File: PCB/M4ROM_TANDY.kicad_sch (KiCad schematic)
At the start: 7 parts, among them J1 Tandy_100_102_200_option_rom, J2 4ROM_prog_female, SW1 CUS-14TB, U1 29F010

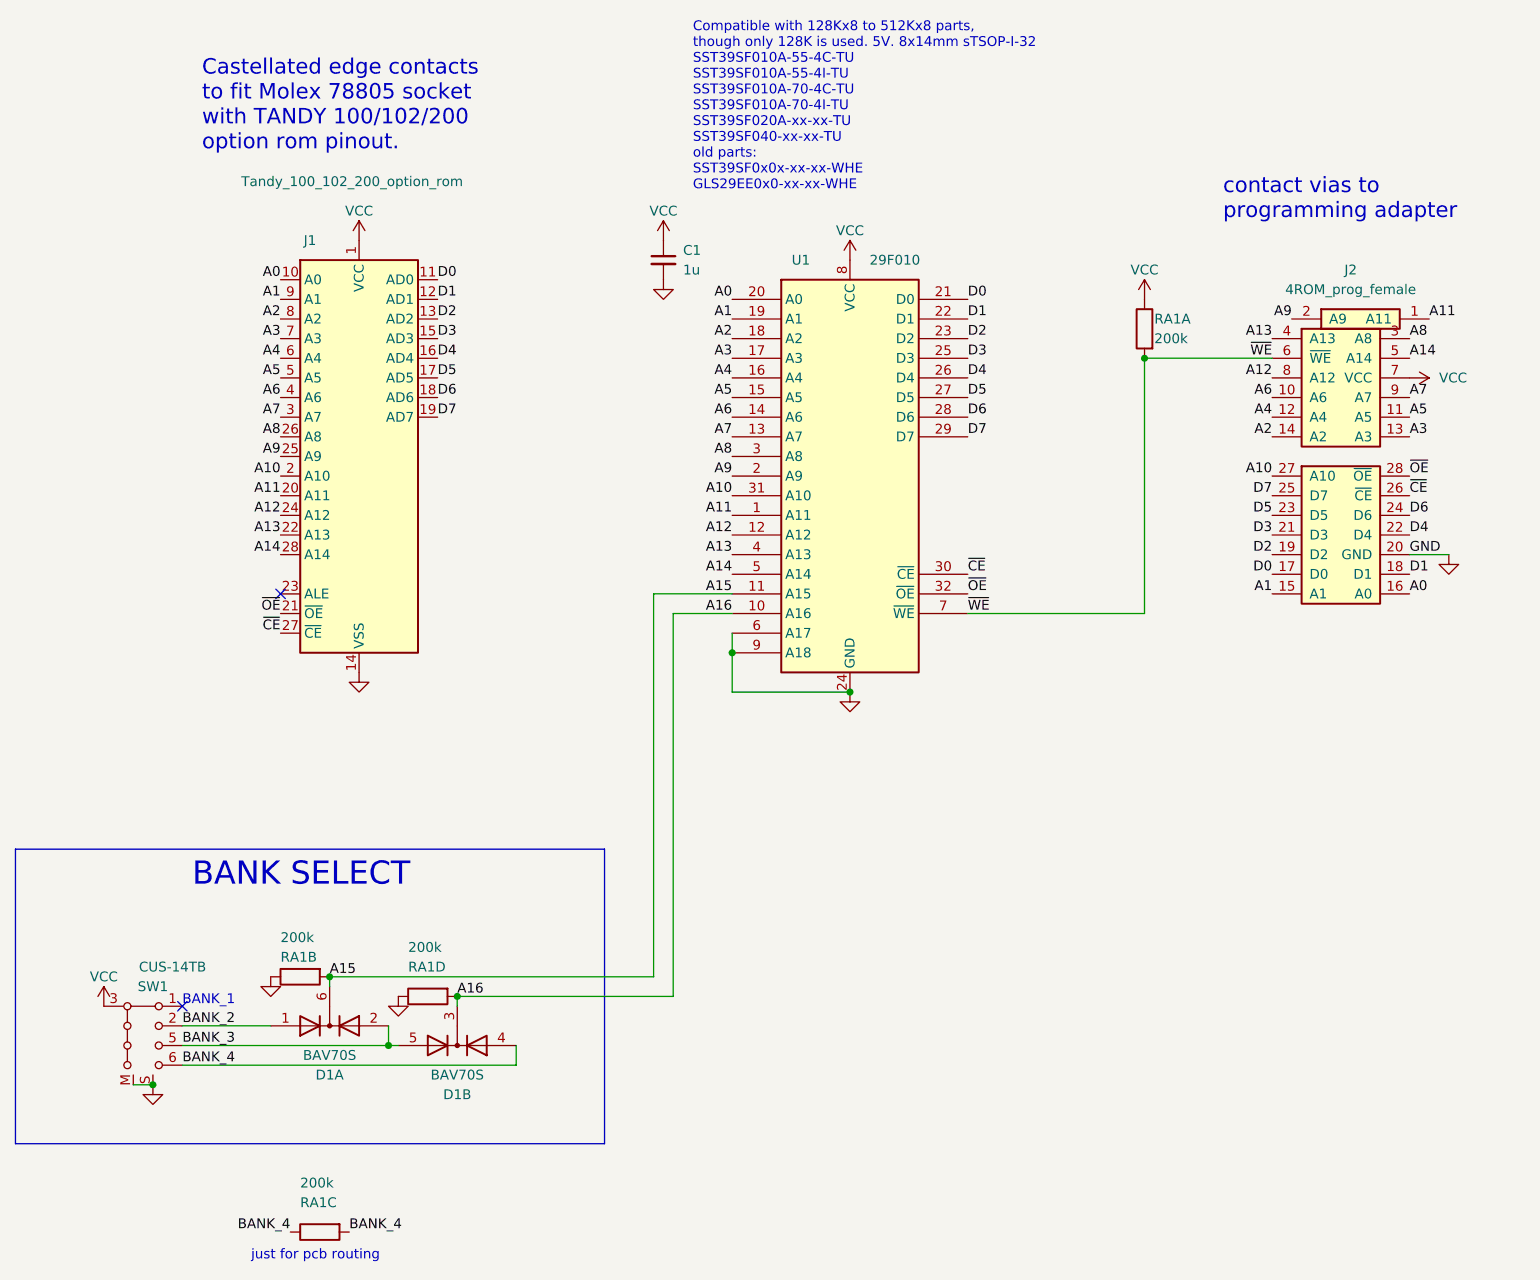
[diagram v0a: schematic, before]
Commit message: simpler diodes
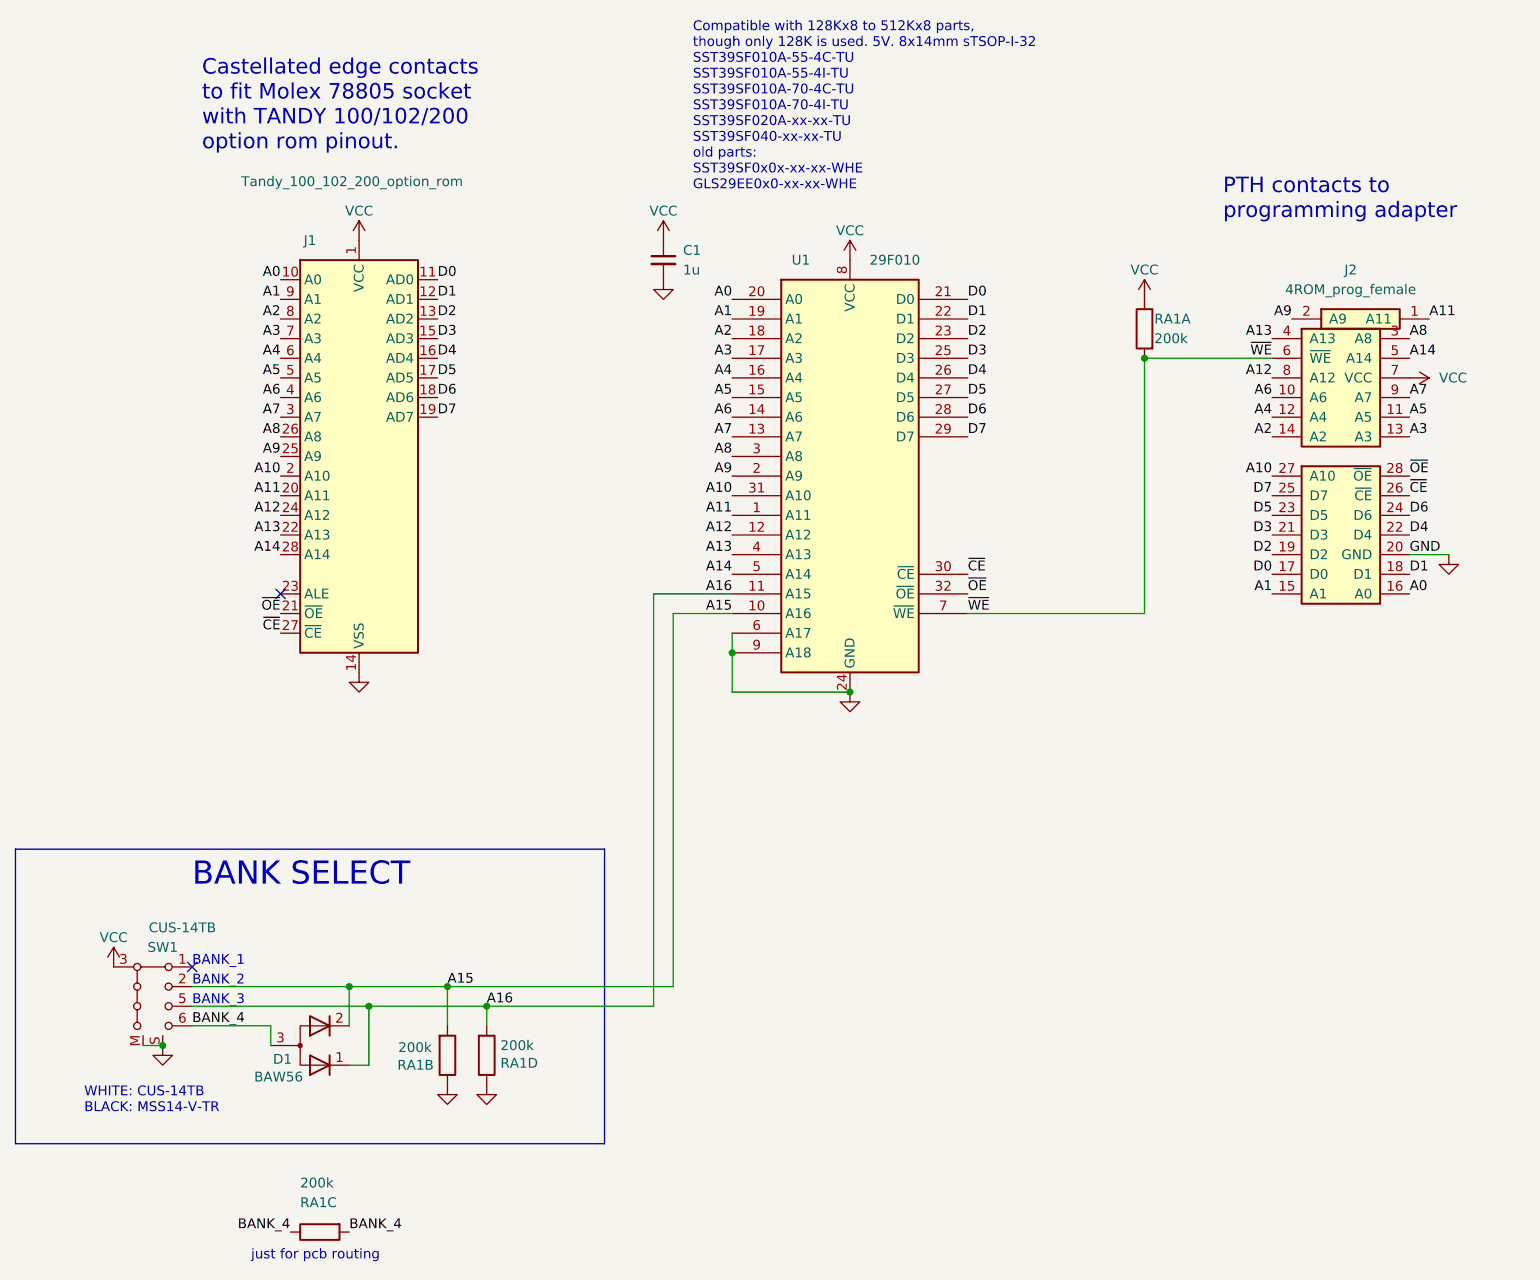
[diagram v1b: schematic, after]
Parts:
- removed D1: BAV70S, 000_LOCAL:TSSOP-6-symmetric, symbol 000_LOCAL:BAV70S
- added D1: BAW56, 000_LOCAL:SOT-23, symbol 000_LOCAL:D_Dual_CommonAnode_KKA_Parallel
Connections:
- net BANK_2 is gone; now on net A15: SW1.2
- net BANK_3 is gone; now on net A16: SW1.5
- net A15: now also U1.10 (A16), D1.2 (K); no longer U1.11 (A15)
- net A16: now also U1.11 (A15), D1.1 (K); no longer U1.10 (A16)
- net BANK_4: now also D1.3 (A)
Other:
- note added: "BANK_2"
- note added: "BANK_3"
- note added: "PTH contacts to programming adapter"
- note added: "WHITE: CUS-14TB BLACK: MSS14-V-TR"
- note removed: "contact vias to programming adapter"
- moved on the sheet: SW1
